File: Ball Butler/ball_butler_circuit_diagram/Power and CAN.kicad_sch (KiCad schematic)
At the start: 12 parts

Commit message: Minor update to schematic
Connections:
- net at U?. (GND): now also U?. (GND); no longer U?. (GND) (x5)
- net at U?. (GND): no longer U?. (GND)
- net at U?. (GND): now also U?. (GND)
- net at U?. (GND): now also U?. (GND), U?. (GND); no longer U?. (GND)
- new net: U?. (GND), U?. (GND), U?. (GND), U?. (GND), U?. (GND), U?. (GND), U?. (GND), U?. (GND), U?. (GND), U?. (GND)
- new net: U?. (GND), U?. (GND), U?. (GND), U?. (GND), U?. (GND), U?. (GND), U?. (GND), U?. (GND)
- new net: U?. (GND), U?. (GND) (x22)
- new net: U?. (GND), U?. (GND), U?. (GND) (x2)
- now unconnected: U?. (GND), U?. (GND), U?. (GND), U?. (GND), U?. (GND), U?. (GND), U?. (GND)
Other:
- note added: "<-- Approx. 2m long -->"

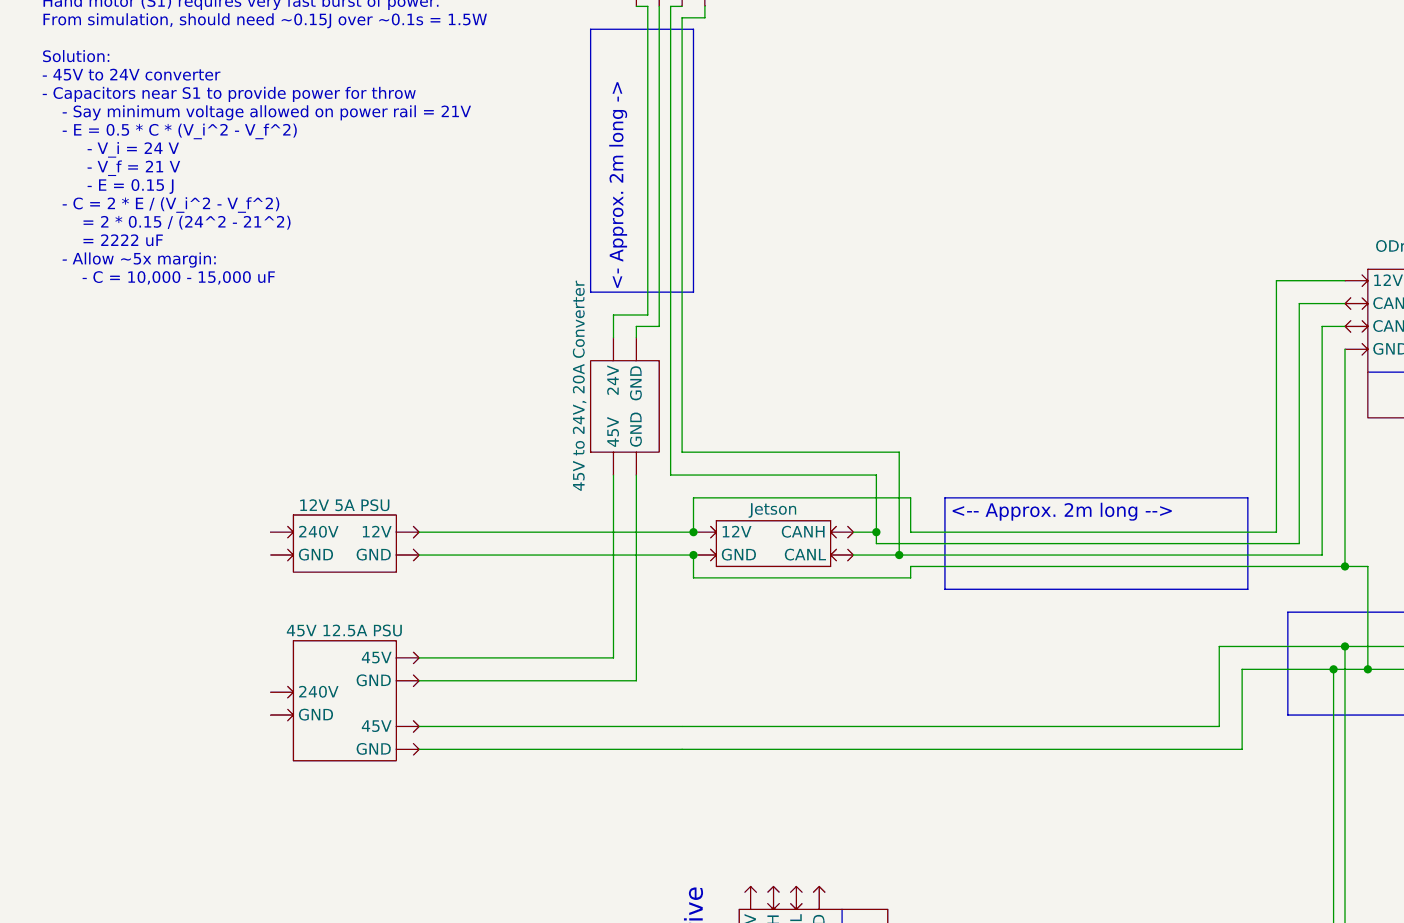
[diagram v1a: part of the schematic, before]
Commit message: Update circuit diagram
Add ROS -> CAN1 = CAN2
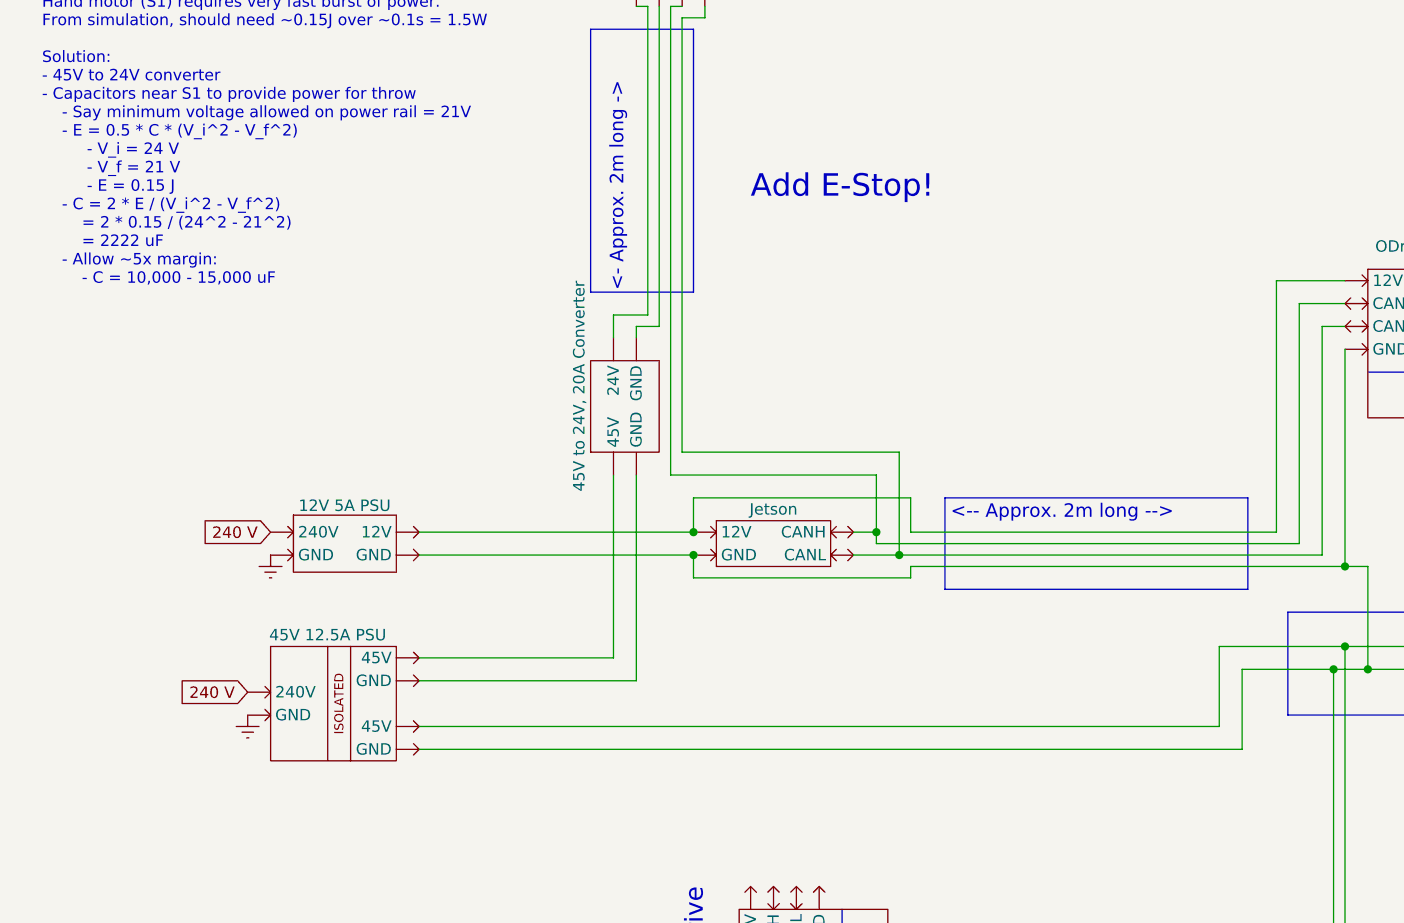
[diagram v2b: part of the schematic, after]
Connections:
- net at U?. (GND): now also U?. (GND); no longer U?. (GND) (x5)
- net at U?. (GND): no longer U?. (GND)
- net Earth: now reaches U?. (GND)
- net Earth: now also U?. (GND)
- net at U?. (GND): now also U?. (GND), U?. (GND); no longer U?. (GND)
- new net: U?. (GND), U?. (GND), U?. (GND), U?. (GND), U?. (GND), U?. (GND), U?. (GND), U?. (GND), U?. (GND), U?. (GND)
- new net: U?. (GND), U?. (GND), U?. (GND), U?. (GND), U?. (GND), U?. (GND), U?. (GND), U?. (GND)
- new net: U?. (GND), U?. (GND) (x23)
- new net: U?. (GND), U?. (GND), U?. (GND) (x2)
- new net 240 V: U?. (GND), U?. (GND)
- now unconnected: U?. (GND), U?. (GND), U?. (GND), U?. (GND), U?. (GND)
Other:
- note added: "Add E-Stop!"
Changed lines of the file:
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@@
     (stroke (width 0.5) (type default) (color 255 0 0 1))
   )
-  (wire (pts (xy 109.22 115.57) (xy 168.91 115.57))
+  (wire (pts (xy 80.01 115.57) (xy 168.91 115.57))
     (stroke (width 0.5) (type default) (color 255 0 0 1))
   )
@@
     (stroke (width 0.5) (type default) (color 0 0 0 1))
   )
-  (wire (pts (xy 109.22 118.11) (xy 171.45 118.11))
-    (stroke (width 0.5) (type default) (color 0 0 0 1))
-  )
   (wire (pts (xy 218.44 97.79) (xy 218.44 106.68))
     (stroke (width 0.5) (type default) (color 255 0 0 1))
@@
     (stroke (width 0.3) (type dash) (color 255 0 0 1))
   )
-  (wire (pts (xy 109.22 115.57) (xy 80.01 115.57))
-    (stroke (width 0) (type default) (color 0 0 0 0))
-  )
   (wire (pts (xy 110.49 99.06) (xy 134.62 99.06))
     (stroke (width 0.3) (type dash) (color 0 0 0 1))
@@
     (stroke (width 0.3) (type dash) (color 255 0 0 1))
   )
-  (wire (pts (xy 109.22 118.11) (xy 80.01 118.11))
-    (stroke (width 0) (type default) (color 0 0 0 0))
+  (wire (pts (xy 80.01 118.11) (xy 171.45 118.11))
+    (stroke (width 0.5) (type default) (color 0 0 0 1))
   )
   (polyline (pts (xy 110.49 67.31) (xy 110.49 38.1))
@@
   (text "BUS BARS" (at 195.58 113.03 0)
     (effects (font (size 1.5 1.5)) (justify left bottom))
+  )
+  (text "Add E-Stop!" (at 116.84 57.15 0)
+    (effects (font (size 2.5 2.5)) (justify left bottom))
   )
   (text "Hand ODrive" (at 111.76 151.13 90)
@@
     (effects (font (size 1.5 1.5)) (justify left bottom))
   )
+  (global_label "240 V" (shape input) (at 63.5 93.98 180) (fields_autoplaced)
+    (effects (font (size 1.27 1.27)) (justify right))
+    (property "Intersheet References" "${INTERSHEET_REFS}" (id 0) (at 55.4021 93.9006 0)
+      (effects (font (size 1.27 1.27)) (justify right) hide)
+    )
+  )
+  (global_label "240 V" (shape input) (at 60.96 111.76 180) (fields_autoplaced)
+    (effects (font (size 1.27 1.27)) (justify right))
+    (property "Intersheet References" "${INTERSHEET_REFS}" (id 0) (at 52.8621 111.6806 0)
+      (effects (font (size 1.27 1.27)) (justify right) hide)
+    )
+  )
   (symbol (lib_id "Power_CAN_Symbol_Library:ODrive Pro") (at 191.77 152.4 180) (unit 1)
     (in_bom yes) (on_board yes) (fields_autoplaced)
@@
       (effects (font (size 1.27 1.27)) hide)
     )
-    (property "Value" "45V 12.5A PSU" (id 1) (at 71.7296 104.9528 0))
+    (property "Value" "45V 12.5A PSU" (id 1) (at 69.85 105.41 0))
     (property "Footprint" "" (id 2) (at 63.5 113.03 0)
       (effects (font (size 1.27 1.27)) hide)
@@
     (pin "")
     (pin "")
+  )
+  (symbol (lib_id "power:Earth") (at 60.96 114.3 0) (unit 1)
+    (in_bom yes) (on_board yes) (fields_autoplaced)
+    (property "Reference" "#PWR?" (id 0) (at 60.96 120.65 0)
+      (effects (font (size 1.27 1.27)) hide)
+    )
+    (property "Value" "Earth" (id 1) (at 60.96 118.11 0)
+      (effects (font (size 1.27 1.27)) hide)
+    )
+    (property "Footprint" "" (id 2) (at 60.96 114.3 0)
+      (effects (font (size 1.27 1.27)) hide)
+    )
+    (property "Datasheet" "~" (id 3) (at 60.96 114.3 0)
+      (effects (font (size 1.27 1.27)) hide)
+    )
+    (pin "1")
   )
   (symbol (lib_id "Power_CAN_Symbol_Library:ODrive Pro") (at 212.09 69.85 0) (unit 1)
@@
     (pin "")
   )
+  (symbol (lib_id "power:Earth") (at 63.5 96.52 0) (unit 1)
+    (in_bom yes) (on_board yes) (fields_autoplaced)
+    (property "Reference" "#PWR?" (id 0) (at 63.5 102.87 0)
+      (effects (font (size 1.27 1.27)) hide)
+    )
+    (property "Value" "Earth" (id 1) (at 63.5 100.33 0)
+      (effects (font (size 1.27 1.27)) hide)
+    )
+    (property "Footprint" "" (id 2) (at 63.5 96.52 0)
+      (effects (font (size 1.27 1.27)) hide)
+    )
+    (property "Datasheet" "~" (id 3) (at 63.5 96.52 0)
+      (effects (font (size 1.27 1.27)) hide)
+    )
+    (pin "1")
+  )
   (symbol (lib_id "Power_CAN_Symbol_Library:ODrive Pro") (at 191.77 69.85 0) (unit 1)

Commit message: Update circuit diagram
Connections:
- net at U?. (GND): now also U?. (GND); no longer U?. (GND) (x5)
- net at U?. (GND): no longer U?. (GND)
- net at U?. (GND): now also U?. (GND), U?. (GND); no longer U?. (GND)
- new net: U?. (GND), U?. (GND), U?. (GND), U?. (GND), U?. (GND), U?. (GND), U?. (GND), U?. (GND), U?. (GND), U?. (GND)
- new net: U?. (GND), U?. (GND), U?. (GND), U?. (GND), U?. (GND), U?. (GND), U?. (GND), U?. (GND)
- new net: U?. (GND), U?. (GND) (x23)
- new net: U?. (GND), U?. (GND), U?. (GND) (x2)
- now unconnected: U?. (GND), U?. (GND), U?. (GND), U?. (GND), U?. (GND)

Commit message: Update Ball Butler schematic
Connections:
- net at U?. (GND): now also U?. (GND); no longer U?. (GND) (x5)
- net at U?. (GND): no longer U?. (GND)
- net at U?. (GND): now also U?. (GND), U?. (GND); no longer U?. (GND)
- new net: U?. (GND), U?. (GND), U?. (GND), U?. (GND), U?. (GND), U?. (GND), U?. (GND), U?. (GND), U?. (GND), U?. (GND)
- new net: U?. (GND), U?. (GND), U?. (GND), U?. (GND), U?. (GND), U?. (GND), U?. (GND), U?. (GND)
- new net: U?. (GND), U?. (GND) (x23)
- new net: U?. (GND), U?. (GND), U?. (GND) (x2)
- now unconnected: U?. (GND), U?. (GND), U?. (GND), U?. (GND), U?. (GND)
